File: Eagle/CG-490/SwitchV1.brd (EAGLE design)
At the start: 36.8 x 28.9 mm, 10 parts, among them IC1 MIC4420N, Q1 IRF540

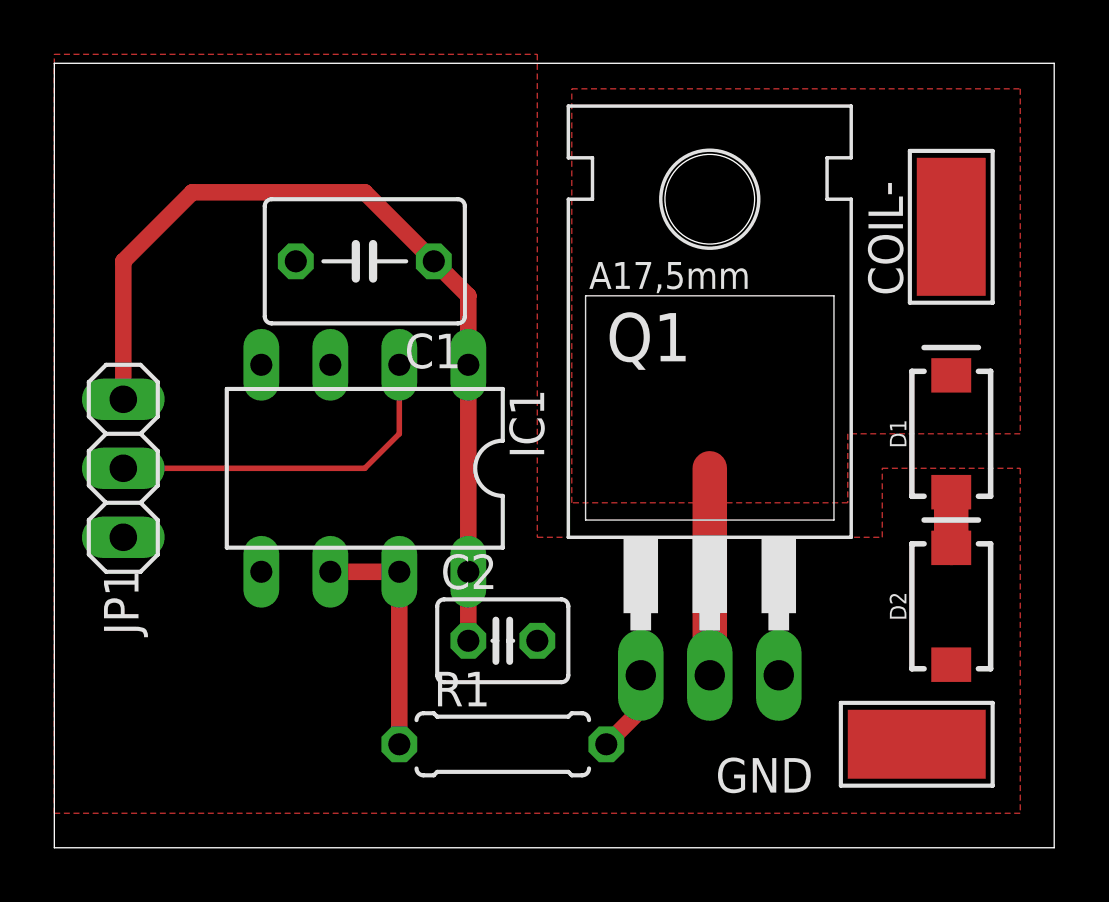
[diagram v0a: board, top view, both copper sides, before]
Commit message: ran simulation of real world stage 1 design, created optical assembly CAD file
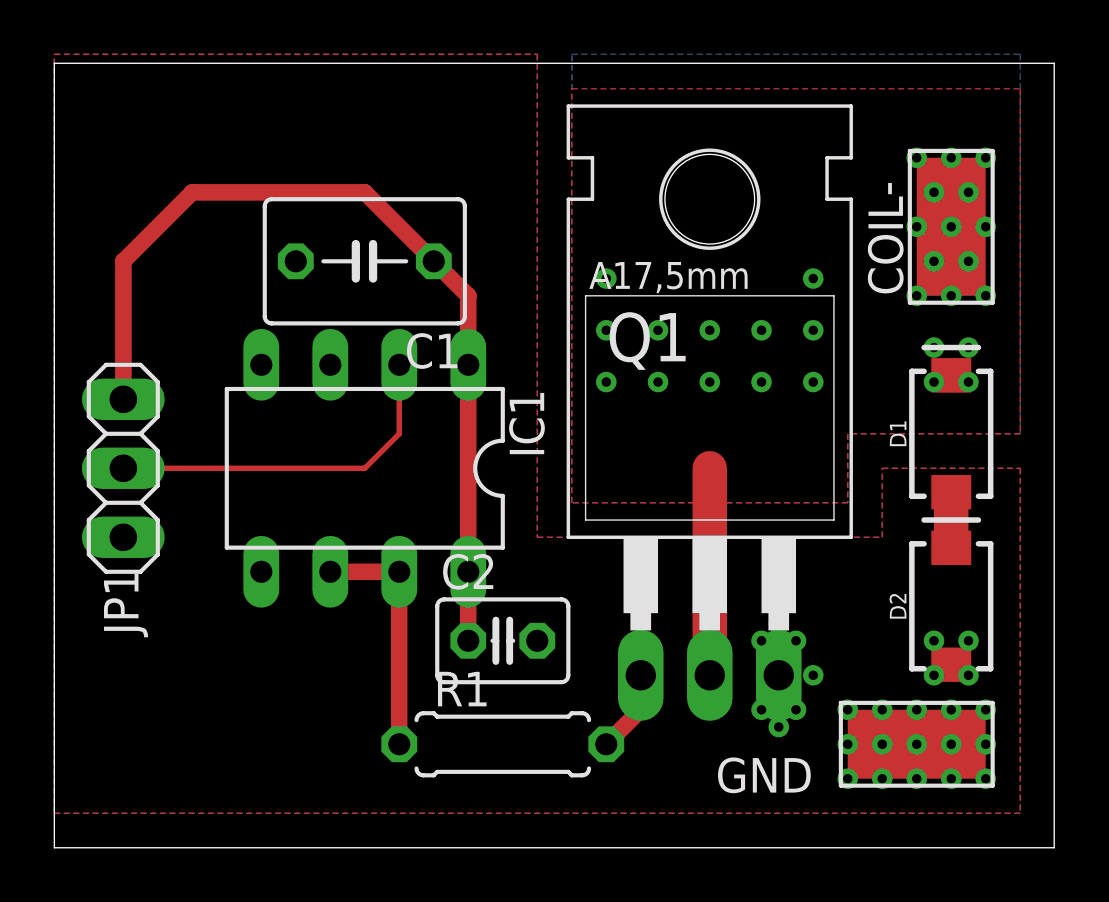
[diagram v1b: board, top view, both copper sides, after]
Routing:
- net OUT: vias 0 -> 29
- added copper zone on layer 16, net GND
- added copper zone on layer 16, net OUT
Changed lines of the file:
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@@
 <setting verticaltext="up"/>
 </settings>
-<grid distance="50" unitdist="mil" unit="mil" style="lines" multiple="1" display="no" altdistance="5" altunitdist="mil" altunit="mil"/>
+<grid distance="25" unitdist="mil" unit="mil" style="lines" multiple="1" display="no" altdistance="5" altunitdist="mil" altunit="mil"/>
 <layers>
 <layer number="1" name="Top" color="4" fill="1" visible="yes" active="yes"/>
@@
 <layer number="27" name="tValues" color="7" fill="1" visible="yes" active="yes"/>
 <layer number="28" name="bValues" color="7" fill="1" visible="yes" active="yes"/>
-<layer number="29" name="tStop" color="7" fill="3" visible="no" active="yes"/>
+<layer number="29" name="tStop" color="7" fill="3" visible="yes" active="yes"/>
 <layer number="30" name="bStop" color="7" fill="6" visible="no" active="yes"/>
 <layer number="31" name="tCream" color="7" fill="4" visible="no" active="yes"/>
@@
 <text x="8.89" y="33.02" size="0.8128" layer="51">SIG</text>
 <text x="8.89" y="30.48" size="0.8128" layer="51">GND</text>
+<rectangle x1="24.13" y1="31.75" x2="34.29" y2="46.99" layer="29"/>
 </plain>
 <attributes>
@@
 <vertex x="5.08" y="20.32"/>
 </polygon>
+<polygon width="0.1524" layer="16" thermals="no">
+<vertex x="5.08" y="48.26"/>
+<vertex x="22.86" y="48.26"/>
+<vertex x="22.86" y="30.48"/>
+<vertex x="35.56" y="30.48"/>
+<vertex x="35.56" y="33.02"/>
+<vertex x="40.64" y="33.02"/>
+<vertex x="40.64" y="20.32"/>
+<vertex x="6.35" y="20.32"/>
+<vertex x="5.08" y="20.32"/>
+</polygon>
+<via x="34.29" y="24.13" extent="1-16" drill="0.35"/>
+<via x="34.29" y="22.86" extent="1-16" drill="0.35"/>
+<via x="35.56" y="24.13" extent="1-16" drill="0.35"/>
+<via x="35.56" y="22.86" extent="1-16" drill="0.35"/>
+<via x="36.83" y="24.13" extent="1-16" drill="0.35"/>
+<via x="36.83" y="22.86" extent="1-16" drill="0.35"/>
+<via x="38.1" y="24.13" extent="1-16" drill="0.35"/>
+<via x="38.1" y="22.86" extent="1-16" drill="0.35"/>
+<via x="39.37" y="24.13" extent="1-16" drill="0.35"/>
+<via x="39.37" y="22.86" extent="1-16" drill="0.35"/>
+<via x="39.37" y="21.59" extent="1-16" drill="0.35"/>
+<via x="38.1" y="21.59" extent="1-16" drill="0.35"/>
+<via x="36.83" y="21.59" extent="1-16" drill="0.35"/>
+<via x="35.56" y="21.59" extent="1-16" drill="0.35"/>
+<via x="34.29" y="21.59" extent="1-16" drill="0.35"/>
+<via x="32.385" y="26.67" extent="1-16" drill="0.35"/>
+<via x="31.115" y="26.67" extent="1-16" drill="0.35"/>
+<via x="31.115" y="24.13" extent="1-16" drill="0.35"/>
+<via x="32.385" y="24.13" extent="1-16" drill="0.35"/>
+<via x="33.02" y="25.4" extent="1-16" drill="0.35"/>
+<via x="31.75" y="27.305" extent="1-16" drill="0.35"/>
+<via x="31.75" y="23.495" extent="1-16" drill="0.35"/>
+<via x="37.465" y="25.4" extent="1-16" drill="0.35"/>
+<via x="38.735" y="25.4" extent="1-16" drill="0.35"/>
+<via x="38.735" y="26.67" extent="1-16" drill="0.35"/>
+<via x="37.465" y="26.67" extent="1-16" drill="0.35"/>
 </signal>
 <signal name="N$1">
@@
 </polygon>
 <wire x1="29.21" y1="25.4" x2="29.21" y2="33.02" width="1.27" layer="1"/>
+<polygon width="0.1524" layer="16">
+<vertex x="24.13" y="31.75"/>
+<vertex x="24.13" y="48.26"/>
+<vertex x="40.64" y="48.26"/>
+<vertex x="40.64" y="34.29"/>
+<vertex x="34.29" y="34.29"/>
+<vertex x="34.29" y="31.75"/>
+</polygon>
+<via x="39.37" y="44.45" extent="1-16" drill="0.35"/>
+<via x="38.1" y="44.45" extent="1-16" drill="0.35"/>
+<via x="36.83" y="44.45" extent="1-16" drill="0.35"/>
+<via x="37.465" y="43.18" extent="1-16" drill="0.35"/>
+<via x="38.735" y="43.18" extent="1-16" drill="0.35"/>
+<via x="39.37" y="41.91" extent="1-16" drill="0.35"/>
+<via x="38.1" y="41.91" extent="1-16" drill="0.35"/>
+<via x="36.83" y="41.91" extent="1-16" drill="0.35"/>
+<via x="37.465" y="40.64" extent="1-16" drill="0.35"/>
+<via x="38.735" y="40.64" extent="1-16" drill="0.35"/>
+<via x="39.37" y="39.37" extent="1-16" drill="0.35"/>
+<via x="38.1" y="39.37" extent="1-16" drill="0.35"/>
+<via x="36.83" y="39.37" extent="1-16" drill="0.35"/>
+<via x="25.4" y="38.1" extent="1-16" drill="0.35"/>
+<via x="27.305" y="38.1" extent="1-16" drill="0.35"/>
+<via x="29.21" y="38.1" extent="1-16" drill="0.35"/>
+<via x="31.115" y="38.1" extent="1-16" drill="0.35"/>
+<via x="33.02" y="38.1" extent="1-16" drill="0.35"/>
+<via x="25.4" y="36.195" extent="1-16" drill="0.35"/>
+<via x="27.305" y="36.195" extent="1-16" drill="0.35"/>
+<via x="29.21" y="36.195" extent="1-16" drill="0.35"/>
+<via x="31.115" y="36.195" extent="1-16" drill="0.35"/>
+<via x="33.02" y="36.195" extent="1-16" drill="0.35"/>
+<via x="33.02" y="40.005" extent="1-16" drill="0.35"/>
+<via x="25.4" y="40.005" extent="1-16" drill="0.35"/>
+<via x="37.465" y="37.465" extent="1-16" drill="0.35"/>
+<via x="38.735" y="37.465" extent="1-16" drill="0.35"/>
+<via x="38.735" y="36.195" extent="1-16" drill="0.35"/>
+<via x="37.465" y="36.195" extent="1-16" drill="0.35"/>
 </signal>
 <signal name="N$4">
